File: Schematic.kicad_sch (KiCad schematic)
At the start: 7 parts, among them SW1 SW_SPST, U1 ATtiny85

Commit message: Chose another board and update files
Updated README.md, modified the size of schematic, add another part of schematic for CH552 and plot the SVG version
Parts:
- added IN1, OUT1: USB_A, symbol Connector:USB_A
- added PMOS1: PMOS_Substrate, symbol Simulation_SPICE:PMOS_Substrate
- added R3: 220, symbol Device:R_US
- added R4: 10k, symbol Device:R_US
- added SW2: SW_SPST, symbol Switch:SW_SPST
- added U2: CH552G, symbol CH552G:CH552G
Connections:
- net Onboard LED: now also U2.8 (P3.0)
- new net: SW2.1 (A), U2.12 (P3.6)
- new net: IN1.4 (GND), OUT1.4 (GND), SW2.2 (B), U2.14 (GND)
- new net: IN1.1 (VBUS), PMOS1.3 (S), R4.2
- new net: IN1.2 (D-), OUT1.2 (D-)
- new net: IN1.3 (D+), OUT1.3 (D+)
- new net: PMOS1.2 (G), R3.2, R4.1
- new net: R3.1, U2.13 (P3.7)
- new net: OUT1.1 (VBUS), PMOS1.1 (D)
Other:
- note added: "ATtiny85 Version"
- note added: "CH552 Version"

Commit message: Basic development completed
The code and the wiring functions, CH552 tested. Wiring graph and more detailed README to be updated.
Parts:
- added C1, C2: 0.1μF, symbol Device:C
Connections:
- net at IN.4 (GND), OUT.4 (GND), SW1.2 (B)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: now also C2.2
- net at SW1.1 (A), U1.7 (PB2): now also C2.1
- net at SW2.1 (A): now also U2.11 (P3.5), C1.1; no longer U2.12 (P3.6)
- net at IN1.4 (GND), OUT1.4 (GND), SW2.2 (B)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: now also C1.2
- net at U2.13 (P3.7): no longer R3.1
- net at U2.9 (P3.3): now also R3.1
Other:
- moved on the sheet: OUT1, PMOS1, SW2

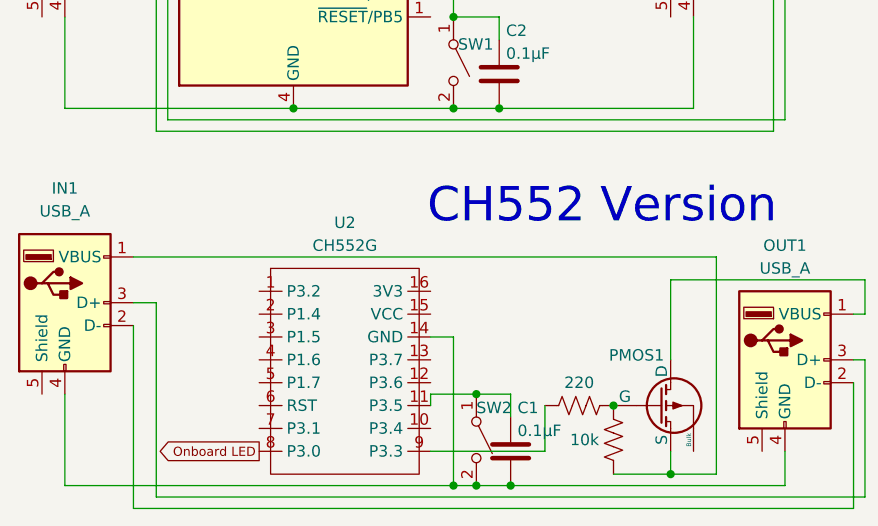
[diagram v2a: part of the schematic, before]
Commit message: Add capacitor to BOM and update schematic
Added a 0.1μF capacitor for hardware debounce to the BOM in README.md. Updated the KiCad schematic and SVG to include the capacitor and its connections.
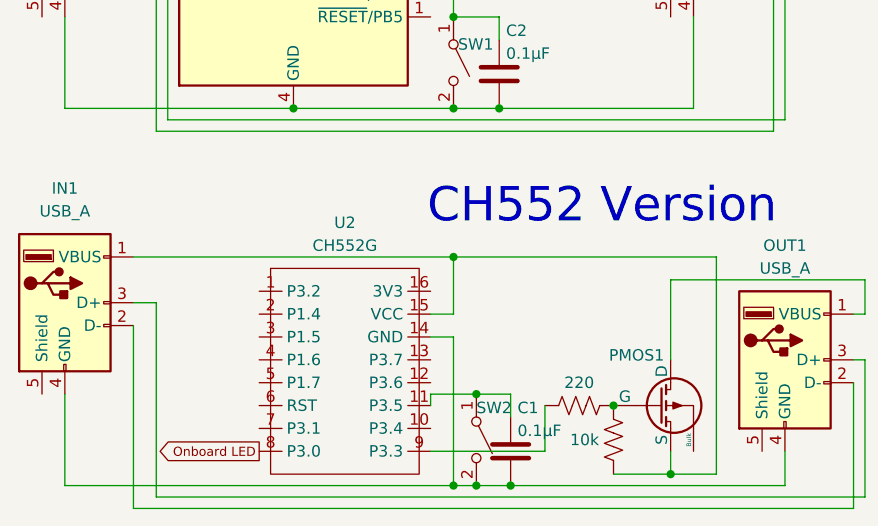
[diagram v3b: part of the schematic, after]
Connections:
- net at IN1.1 (VBUS), PMOS1.3 (S), R4.2: now also U2.15 (VCC)
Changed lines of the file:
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@@
+	)
+	(junction
+		(at 64.77 69.85)
+		(diameter 0)
+		(color 0 0 0 0)
 	)
 	(junction
@@
 	(wire
 		(pts
+			(xy 62.23 76.2) (xy 64.77 76.2)
+		)
+		(stroke
+			(width 0)
+			(type default)
+		)
+	)
+	(wire
+		(pts
 			(xy 88.9 72.39) (xy 88.9 81.28)
 		)
@@
 	(wire
 		(pts
+			(xy 64.77 69.85) (xy 93.98 69.85)
+		)
+		(stroke
+			(width 0)
+			(type default)
+		)
+	)
+	(wire
+		(pts
 			(xy 83.82 40.64) (xy 83.82 22.86)
 		)
@@
 	(wire
 		(pts
-			(xy 29.21 69.85) (xy 93.98 69.85)
+			(xy 29.21 69.85) (xy 64.77 69.85)
 		)
 		(stroke
@@
 		)
 		(stroke
+			(width 0)
+			(type default)
+		)
+	)
+	(wire
+		(pts
+			(xy 64.77 76.2) (xy 64.77 69.85)
+		)
+		(stroke

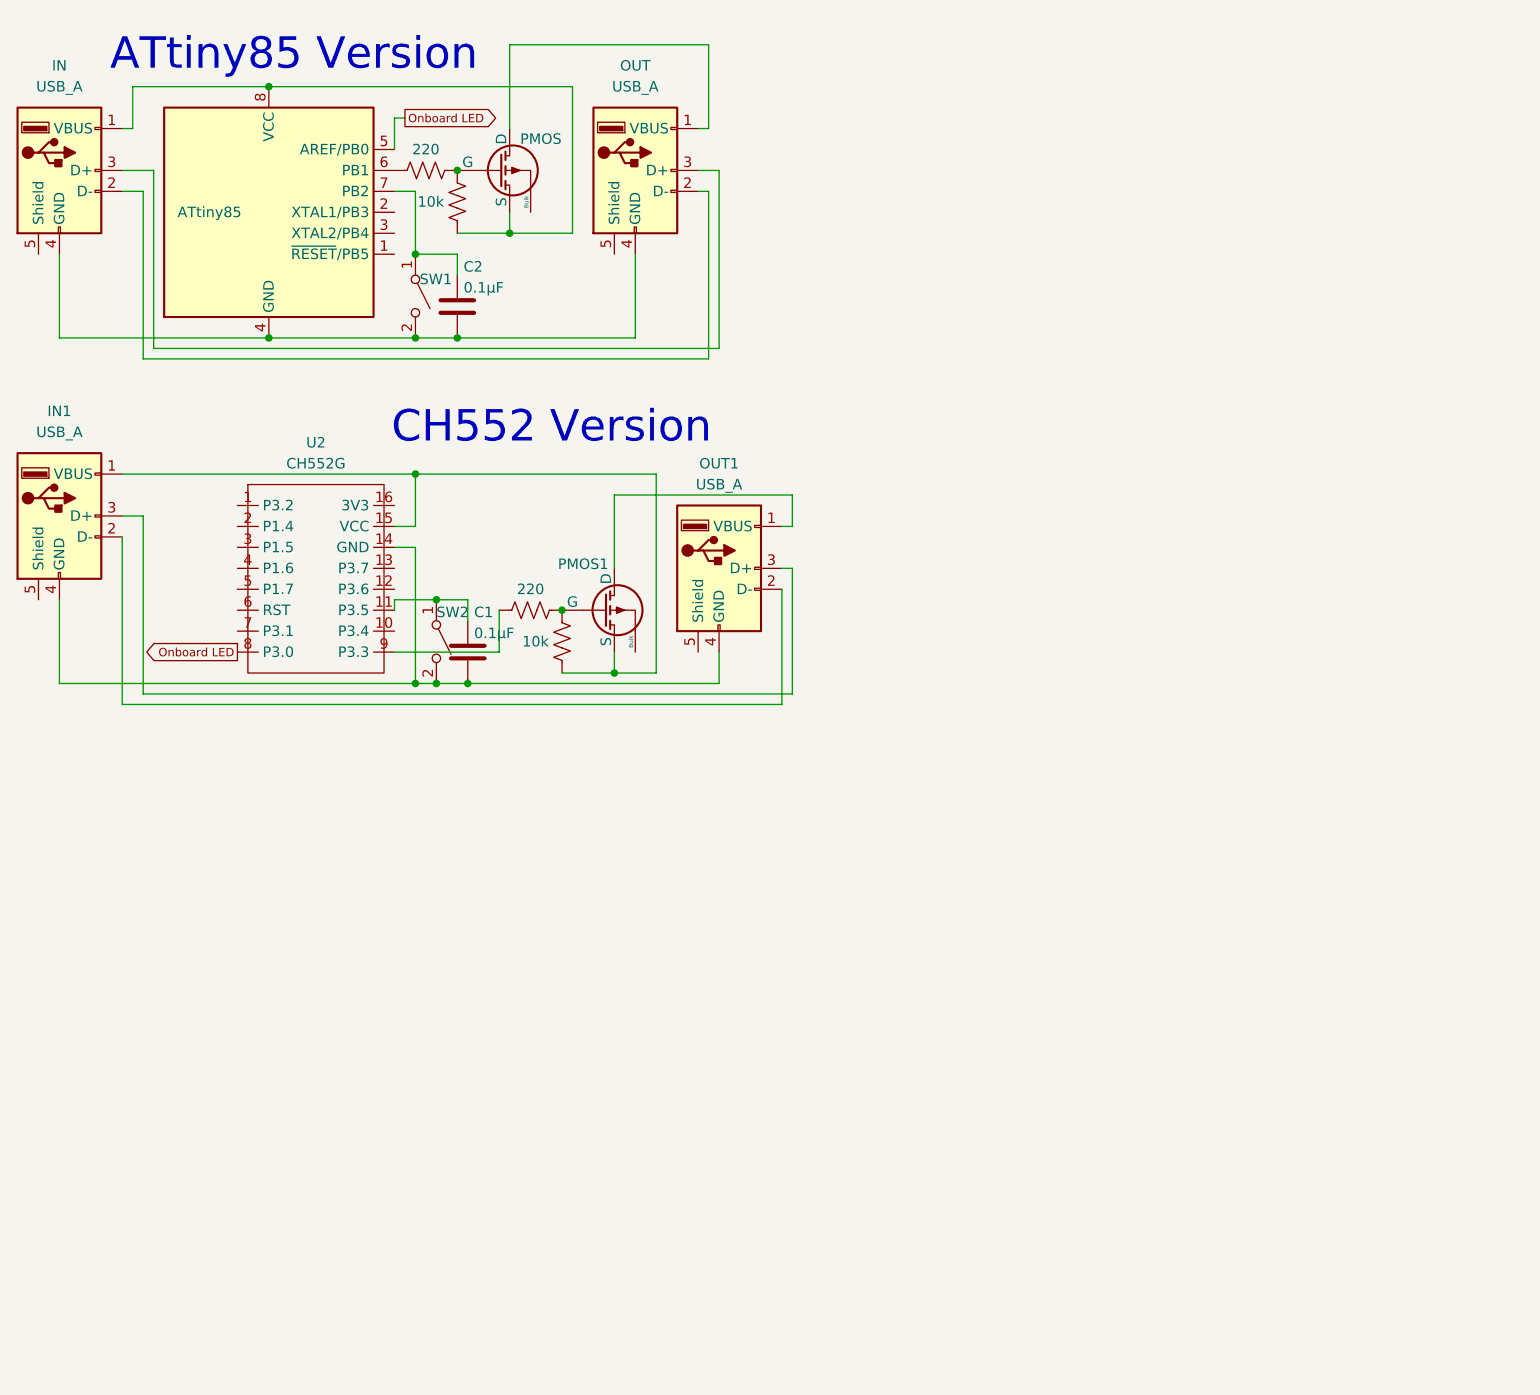
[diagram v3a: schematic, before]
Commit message: Add ESP32C3 SuperMini version to schematic
Also updated the schematic  SVG output to reflect this change.
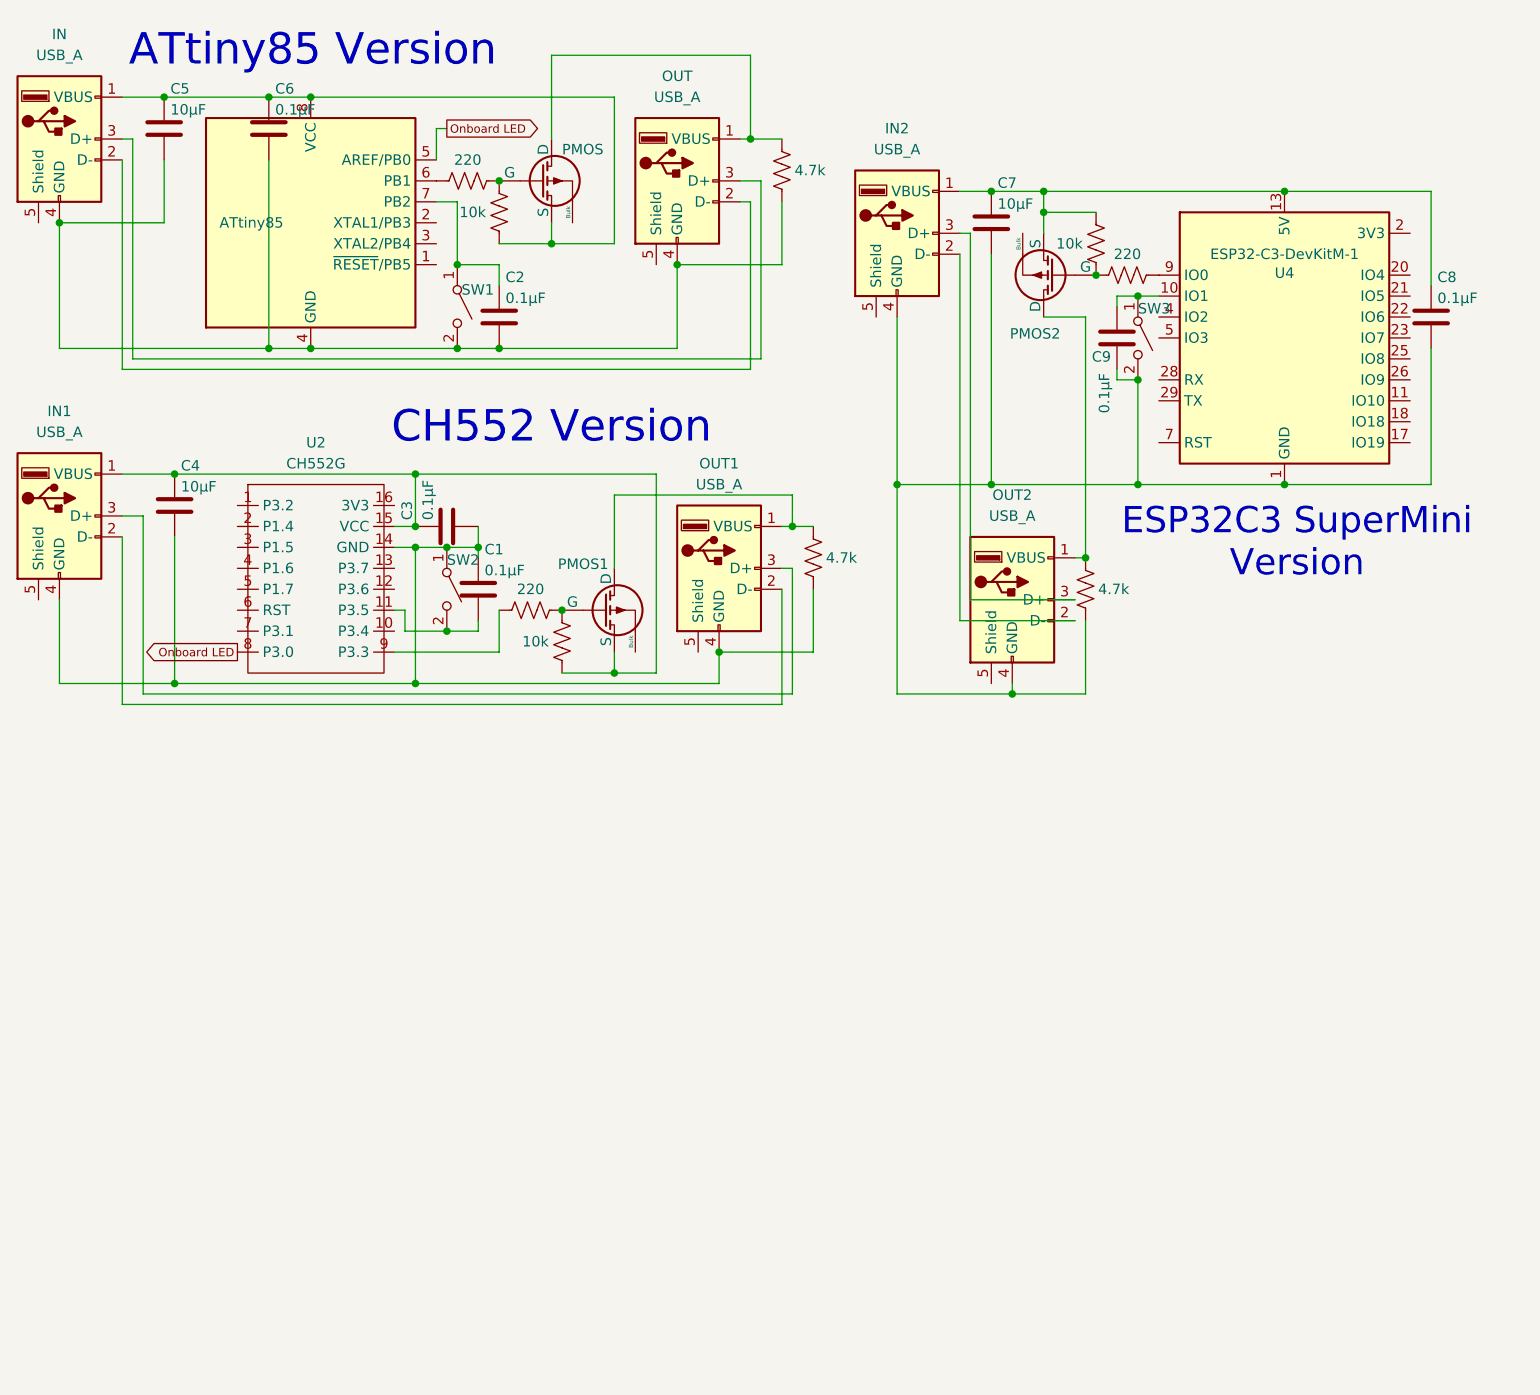
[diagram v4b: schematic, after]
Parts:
- added C3, C6, C8, C9: 0.1μF, symbol Device:C
- added C4, C5, C7: 10μF, symbol Device:C
- added IN2, OUT2: USB_A, symbol Connector:USB_A
- added PMOS2: PMOS_Substrate, symbol Simulation_SPICE:PMOS_Substrate
- added R5, R6, R9: 4.7k, symbol Device:R_US
- added R7: 220, symbol Device:R_US
- added R8: 10k, symbol Device:R_US
- added SW3: SW_SPST, symbol Switch:SW_SPST
- added U4: ESP32-C3-DevKitM-1, RF_Module:ESP32-C3-DevKitM-1, symbol RF_Module:ESP32-C3-DevKitM-1
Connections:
- net at C2.2, IN.4 (GND), OUT.4 (GND)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: now also C5.2, C6.2, R6.2
- net at IN.1 (VBUS), PMOS.3 (S), R2.2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: now also C5.1, C6.1
- net at C1.1, SW2.1 (A): now also IN1.4 (GND), OUT1.4 (GND), U2.14 (GND), C3.2, C4.2, R5.2; no longer U2.11 (P3.5)
- net at IN1.1 (VBUS), PMOS1.3 (S), R4.2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: now also C3.1, C4.1
- net at OUT.1 (VBUS), PMOS.1 (D): now also R6.1
- net at OUT1.1 (VBUS), PMOS1.1 (D): now also R5.1
- new net: C7.1, C8.1, IN2.1 (VBUS), PMOS2.3 (S), R8.1, U4.13 (5V), U4.14 (5V)
- new net: IN2.2 (D-), OUT2.2 (D-)
- new net: IN2.3 (D+), OUT2.3 (D+)
- new net: C7.2, C8.2, C9.2, IN2.4 (GND), OUT2.4 (GND), R9.2, SW3.2 (B), U4.1 (GND), U4.12 (GND), U4.15 (GND), U4.16 (GND), U4.19 (GND), U4.24 (GND), U4.27 (GND), U4.30 (GND), U4.6 (GND), U4.8 (GND)
- new net: C1.2, SW2.2 (B), U2.11 (P3.5)
- new net: OUT2.1 (VBUS), PMOS2.1 (D), R9.1
- new net: C9.1, SW3.1 (A), U4.10 (IO1)
- new net: U4.2 (3V3), U4.3 (3V3)
- new net: R7.2, U4.9 (IO0)
- new net: PMOS2.2 (G), R7.1, R8.2
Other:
- note added: "ESP32C3 SuperMini Version"
- moved on the sheet: C1, C2, IN, OUT, PMOS, SW1, SW2

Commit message: Add perfboard wiring images and update schematic
Added new perfboard wiring images (PNG, SVG, and vector file) and moved schematic files into a dedicated directory.
Updated the main Arduino sketch to add analog loopback output checking
Updated the KiCad schematic
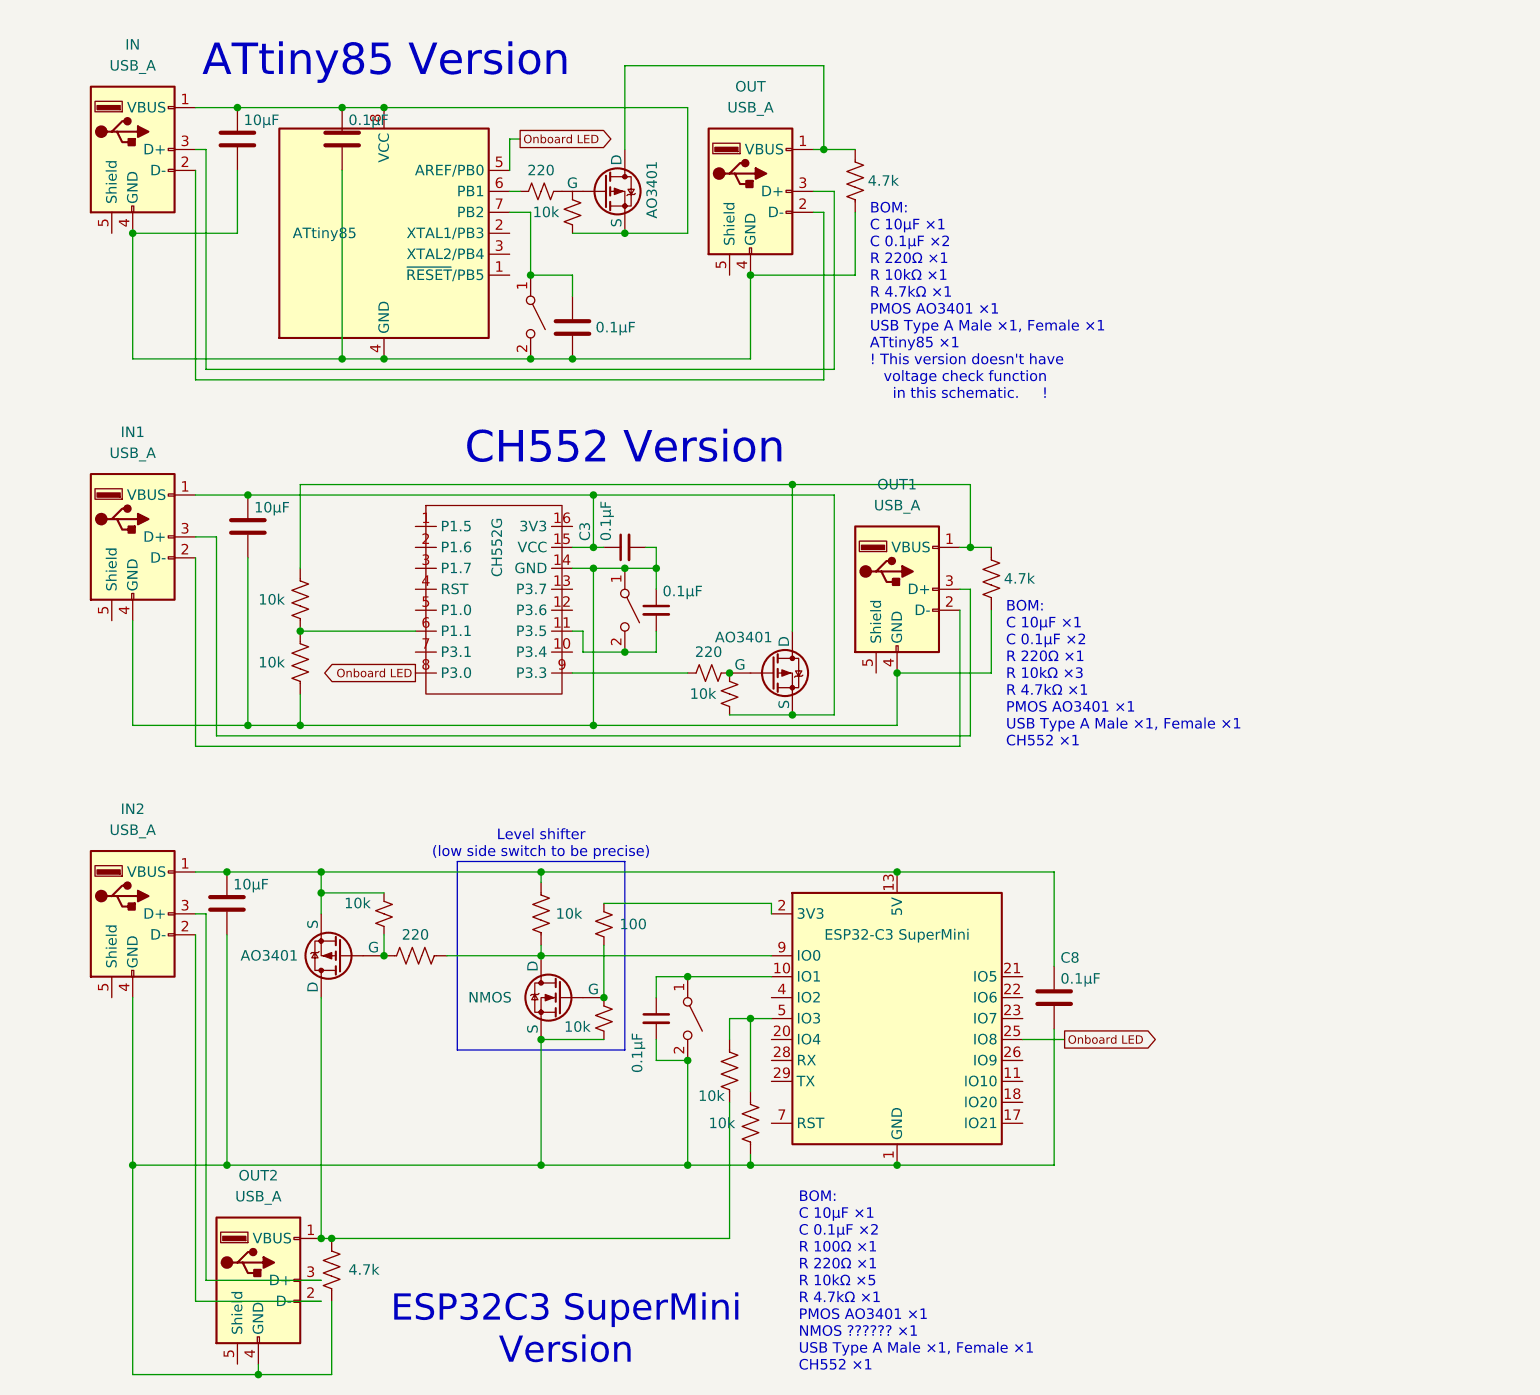
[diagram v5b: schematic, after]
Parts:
- added Q1: NMOS, symbol Simulation_SPICE:NMOS
- added R10, R12, R14, R15, R16: 10k, symbol Device:R_US
- added R11: 100, symbol Device:R_Small_US
- added R13: 10k, symbol Device:R_Small_US
- C1, C3, C9: symbol Device:C -> Device:C_Small
- PMOS, PMOS1, PMOS2: value PMOS_Substrate -> AO3401; symbol Simulation_SPICE:PMOS_Substrate -> Simulation_SPICE:PMOS
- R1, R2, R3, R4, R8: symbol Device:R_US -> Device:R_Small_US
- U4: value ESP32-C3-DevKitM-1 -> ESP32-C3 SuperMini
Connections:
- net Onboard LED: now also U4.25 (IO8)
- net at PMOS.2 (G), R1.2: no longer R2.1
- net at C7.1, C8.1, IN2.1 (VBUS)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: now also R10.1
- net at C7.2, C8.2, C9.2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: now also Q1.3 (S), R13.2, R16.2
- net at C1.1, C3.2, C4.2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: now also R14.2
- net at OUT2.1 (VBUS), PMOS2.1 (D), R9.1: now also R15.2
- net at U4.2 (3V3), U4.3 (3V3): now also R11.1
- net at U4.5 (IO3): now also R15.1, R16.1
- net at R7.2, U4.9 (IO0): now also Q1.1 (D), R10.2
- net at U2.6 (P1.1): now also R12.2, R14.1
- net at OUT1.1 (VBUS), PMOS1.1 (D), R5.1: now also R12.1
- new net: Q1.2 (G), R11.2, R13.1
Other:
- note added: "BOM: C 10μF ×1 C 0.1μF ×2 R 100Ω ×1 R 220Ω ×1 R 10kΩ ×5 R 4.7kΩ ×1 PMOS AO3401 ×1 NMOS ?????? ×1 USB Type A Male ×1, Female ×1 CH552 ×1"
- note added: "BOM: C 10μF ×1 C 0.1μF ×2 R 220Ω ×1 R 10kΩ ×1 R 4.7kΩ ×1 PMOS AO3401 ×1 USB Type A Male ×1, Female ×1 ATtiny85 ×1 ! This version doesn't have voltage check function in this schematic. !"
- note added: "BOM: C 10μF ×1 C 0.1μF ×2 R 220Ω ×1 R 10kΩ ×3 R 4.7kΩ ×1 PMOS AO3401 ×1 USB Type A Male ×1, Female ×1 CH552 ×1"
- note added: "Level shifter (low side switch to be precise)"
- moved on the sheet: C3, C8, IN, IN1, IN2, OUT, OUT1, OUT2
